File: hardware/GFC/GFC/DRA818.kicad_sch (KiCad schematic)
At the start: 28 parts

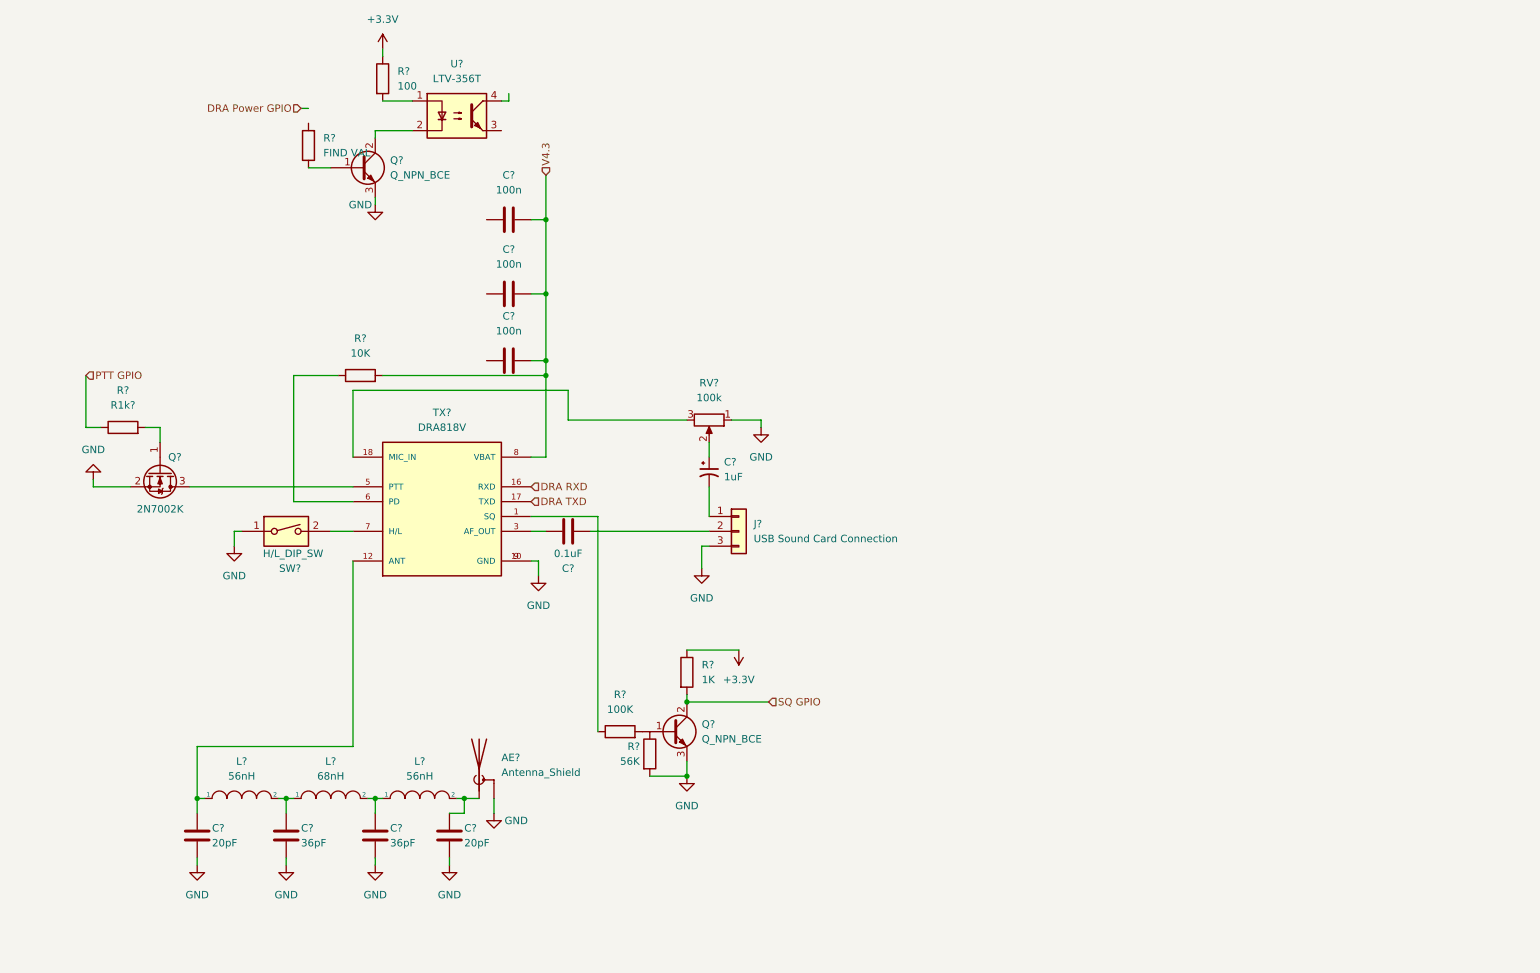
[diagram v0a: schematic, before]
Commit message: Some hardware changes, started to add footprints and part links to digikey. Switching most to SMD
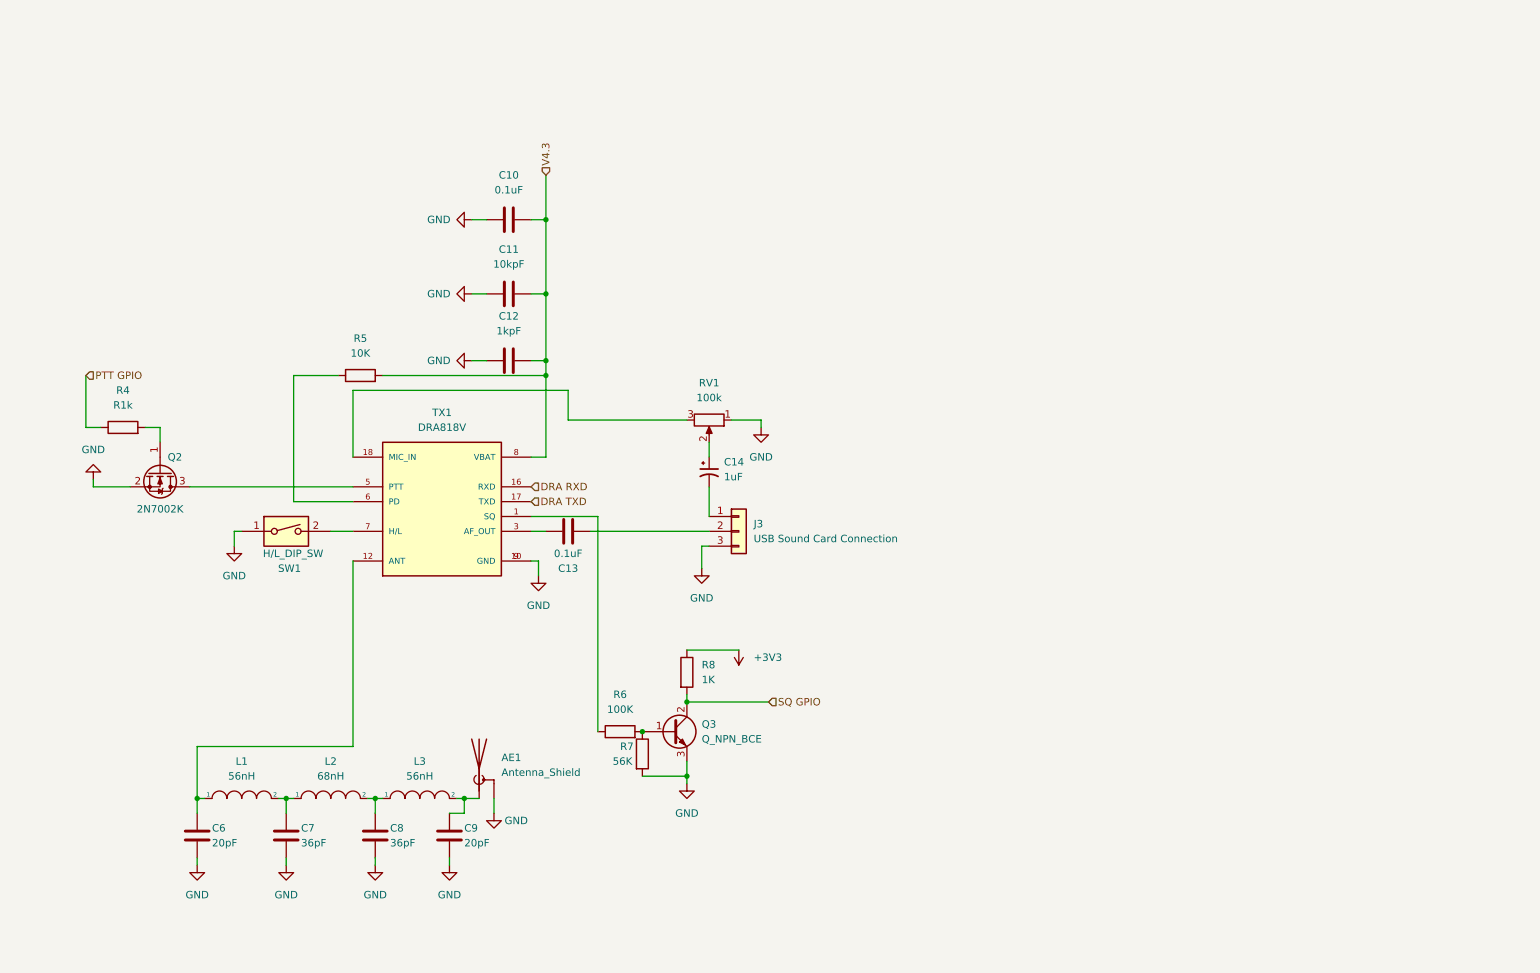
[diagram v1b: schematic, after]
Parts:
- removed Q?: Q_NPN_BCE, symbol Device:Q_NPN_BCE
- removed R?: 100, symbol Device:R
- removed R?: FIND VAL, symbol Device:R
- removed U?: LTV-356T, Package_SO:SO-4_4.4x3.6mm_P2.54mm, symbol Isolator:LTV-356T
- AE1: renamed from AE?; footprint (none) -> footprints:LINX_CONSMA001-G; Digikey (none) -> https://www.digikey.com/en/products/detail/linx-technologie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; Unit Price (none) -> 4.79
- C10: renamed from C?; value 100n -> 0.1uF; footprint (none) -> Capacitor_SMD:C_0603_1608Metric_Pad1.08x0.95mm_HandSolder; Digikey (none) -> https://www.digikey.com/short/3wn2fdb2; Unit Price (none) -> 0.10
- C11: renamed from C?; value 100n -> 10kpF; footprint (none) -> Capacitor_SMD:C_0603_1608Metric_Pad1.08x0.95mm_HandSolder; Digikey (none) -> https://www.digikey.com/short/0b20twhm; Unit Price (none) -> 0.10
- C12: renamed from C?; value 100n -> 1kpF; footprint (none) -> Capacitor_SMD:C_0603_1608Metric_Pad1.08x0.95mm_HandSolder; Digikey (none) -> https://www.digikey.com/short/wt1rq83j; Unit Price (none) -> 0.10
- C13: renamed from C?; footprint (none) -> Capacitor_SMD:C_0603_1608Metric_Pad1.08x0.95mm_HandSolder; Digikey (none) -> https://www.digikey.com/short/3wn2fdb2; Unit Price (none) -> 0.10
- C14: renamed from C?; footprint (none) -> Capacitor_SMD:C_0603_1608Metric_Pad1.08x0.95mm_HandSolder; Digikey (none) -> https://www.digikey.com/short/mb0p55bt; Unit Price (none) -> 0.10
- C6, C9: renamed from C?; footprint (none) -> Capacitor_SMD:C_0603_1608Metric_Pad1.08x0.95mm_HandSolder; Digikey (none) -> https://www.digikey.com/short/fmjn8mbp; Unit Price (none) -> 0.10
- C7, C8: renamed from C?; footprint (none) -> Capacitor_SMD:C_0603_1608Metric_Pad1.08x0.95mm_HandSolder; Digikey (none) -> https://www.digikey.com/short/327pncbq; Unit Price (none) -> 0.10
- J3: renamed from J?; footprint (none) -> Connector_PinHeader_2.54mm:PinHeader_1x03_P2.54mm_Vertical; Digikey (none) -> Already Have
- L1, L3: renamed from L?; footprint (none) -> footprints:IND_AIAC-1812-33NK-T; Digikey (none) -> https://www.digikey.com/short/9vrrnz3q; Unit Price (none) -> .67
- L2: renamed from L?; footprint (none) -> footprints:IND_AIAC-1812-33NK-T; Digikey (none) -> https://www.digikey.com/short/p9jjjhfr; Unit Price (none) -> .63
- Q2: renamed from Q?; footprint Package_TO_SOT_SMD:SOT-23 -> (none)
- R4: renamed from R?; value R1k? -> R1k; Field4 http://www.diygoodies.org.ua/wp-content/uploads/2017/11/Sch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 -> (none)
- RV1: renamed from RV?; footprint (none) -> footprints:TRIM_3361P-1-104GLF; Digikey (none) -> https://www.digikey.com/short/vp58mvrf
- SW1: renamed from SW?; footprint (none) -> Button_Switch_THT:SW_DIP_SPSTx01_Slide_6.7x4.1mm_W7.62mm_P2.54mm_LowProfile; Digikey (none) -> https://www.digikey.com/short/hh7p03qq; Unit Price (none) -> 0.42
- TX1: renamed from TX?; footprint DORJI_DRA818V -> footprints:DORJI_DRA818V; Digikey (none) -> eBay; Unit Price (none) -> 12.28
- gave numbers to parts that had none: 5
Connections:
- net GND: now also C10.1, C11.1, C12.1
- net at Q3.1 (B), R6.2: now also R7.1
- net +3.3V renamed +3V3
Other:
- moved on the sheet: R7

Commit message: Updated footprints - Started work on PCB layout
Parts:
- Q2: value 2N7002K -> DMN67D8LW-13; footprint (none) -> Package_TO_SOT_SMD:SOT-323_SC-70_Handsoldering; Digikey (none) -> https://www.digikey.com/short/vpj3wh87; Unit Price (none) -> 0.26
- Q3: footprint (none) -> Package_TO_SOT_SMD:SOT-23; Digikey (none) -> https://www.digikey.com/short/b477vdt4; Unit Price (none) -> $0.18
- R4: value R1k -> 10k; footprint (none) -> Resistor_SMD:R_0805_2012Metric_Pad1.20x1.40mm_HandSolder; Digikey (none) -> https://www.digikey.com/short/qp0zwmnj; Unit Price (none) -> 0.10
- R5: footprint (none) -> Resistor_SMD:R_0805_2012Metric_Pad1.20x1.40mm_HandSolder; Digikey (none) -> https://www.digikey.com/short/qp0zwmnj; Unit Price (none) -> 0.10
- R6: footprint (none) -> Resistor_SMD:R_0603_1608Metric_Pad0.98x0.95mm_HandSolder; Digikey (none) -> https://www.digikey.com/short/djq9jdpp; Unit Price (none) -> 0.10
- R7: footprint (none) -> Resistor_SMD:R_0603_1608Metric_Pad0.98x0.95mm_HandSolder; Digikey (none) -> https://www.digikey.com/short/bj31bf3h; Unit Price (none) -> 0.10
- R8: footprint (none) -> Resistor_SMD:R_0603_1608Metric_Pad0.98x0.95mm_HandSolder; Digikey (none) -> https://www.digikey.com/short/f10jtr77; Unit Price (none) -> 0.10
- RV1: Unit Price (none) -> 1.27
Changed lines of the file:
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@@
     (stroke (width 0) (type default) (color 0 0 0 0))
   )
-  (wire (pts (xy 33.02 99.06) (xy 39.37 99.06))
+  (wire (pts (xy 25.4 99.06) (xy 39.37 99.06))
     (stroke (width 0) (type default) (color 0 0 0 0))
   )
@@
   )
   (wire (pts (xy 66.04 152.4) (xy 67.31 152.4))
-    (stroke (width 0) (type default) (color 0 0 0 0))
-  )
-  (wire (pts (xy 33.02 99.06) (xy 33.02 97.79))
     (stroke (width 0) (type default) (color 0 0 0 0))
   )
@@
       (effects (font (size 1.27 1.27)) (justify left))
     )
-    (property "Footprint" "" (id 2) (at 132.842 130.81 90)
+    (property "Footprint" "Resistor_SMD:R_0603_1608Metric_Pad0.98x0.95mm_HandSolder" (id 2) (at 132.842 130.81 90)
       (effects (font (size 1.27 1.27)) hide)
     )
     (property "Datasheet" "~" (id 3) (at 134.62 130.81 0)
+      (effects (font (size 1.27 1.27)) hide)
+    )
+    (property "Digikey" "https://www.digikey.com/short/f10jtr77" (id 4) (at 134.62 130.81 0)
+      (effects (font (size 1.27 1.27)) hide)
+    )
+    (property "Unit Price" "0.10" (id 5) (at 134.62 130.81 0)
       (effects (font (size 1.27 1.27)) hide)
     )
@@
     (property "Reference" "R6" (id 0) (at 123.19 134.62 90))
     (property "Value" "100K" (id 1) (at 123.19 137.16 90))
-    (property "Footprint" "" (id 2) (at 123.19 142.748 90)
+    (property "Footprint" "Resistor_SMD:R_0603_1608Metric_Pad0.98x0.95mm_HandSolder" (id 2) (at 123.19 142.748 90)
       (effects (font (size 1.27 1.27)) hide)
     )
     (property "Datasheet" "~" (id 3) (at 123.19 140.97 0)
+      (effects (font (size 1.27 1.27)) hide)
+    )
+    (property "Digikey" "https://www.digikey.com/short/djq9jdpp" (id 4) (at 123.19 140.97 0)
+      (effects (font (size 1.27 1.27)) hide)
+    )
+    (property "Unit Price" "0.10" (id 5) (at 123.19 140.97 0)
       (effects (font (size 1.27 1.27)) hide)
     )
@@
       (effects (font (size 1.27 1.27)) hide)
     )
+    (property "Unit Price" "1.27" (id 5) (at 138.43 87.63 0)
+      (effects (font (size 1.27 1.27)) hide)
+    )
     (pin "1")
     (pin "2")
@@
     (property "Reference" "R5" (id 0) (at 78.74 73.66 90))
     (property "Value" "10K" (id 1) (at 78.74 76.2 90))
-    (property "Footprint" "" (id 2) (at 78.74 81.788 90)
+    (property "Footprint" "Resistor_SMD:R_0805_2012Metric_Pad1.20x1.40mm_HandSolder" (id 2) (at 78.74 81.788 90)
       (effects (font (size 1.27 1.27)) hide)
     )
@@
       (effects (font (size 1.27 1.27)) hide)
     )
+    (property "Digikey" "https://www.digikey.com/short/qp0zwmnj" (id 4) (at 78.74 80.01 0)
+      (effects (font (size 1.27 1.27)) hide)
+    )
+    (property "Unit Price" "0.10" (id 5) (at 78.74 80.01 0)
+      (effects (font (size 1.27 1.27)) hide)
+    )
     (pin "1")
     (pin "2")
@@
     (in_bom yes) (on_board yes)
     (property "Reference" "Q2" (id 0) (at 46.99 93.98 90))
-    (property "Value" "2N7002K" (id 1) (at 44.45 102.87 90))
-    (property "Footprint" "" (id 2) (at 42.545 101.6 0)
+    (property "Value" "DMN67D8LW-13" (id 1) (at 44.45 102.87 90))
+    (property "Footprint" "Package_TO_SOT_SMD:SOT-323_SC-70_Handsoldering" (id 2) (at 42.545 101.6 0)
       (effects (font (size 1.27 1.27) italic) (justify left) hide)
     )
     (property "Datasheet" "https://www.diodes.com/assets/Datasheets/ds30896.pdf" (id 3) (at 44.45 96.52 0)
       (effects (font (size 1.27 1.27)) (justify left) hide)
+    )
+    (property "Digikey" "https://www.digikey.com/short/vpj3wh87" (id 4) (at 44.45 96.52 0)
+      (effects (font (size 1.27 1.27)) hide)
+    )
+    (property "Unit Price" "0.26" (id 5) (at 44.45 96.52 0)
+      (effects (font (size 1.27 1.27)) hide)
     )
     (pin "1")
@@
       (effects (font (size 1.27 1.27)) (justify left))
     )
-    (property "Footprint" "" (id 2) (at 137.16 138.43 0)
+    (property "Footprint" "Package_TO_SOT_SMD:SOT-23" (id 2) (at 137.16 138.43 0)
       (effects (font (size 1.27 1.27)) hide)
     )
@@
       (effects (font (size 1.27 1.27)) hide)
     )
+    (property "Digikey" "https://www.digikey.com/short/b477vdt4" (id 4) (at 132.08 140.97 0)
+      (effects (font (size 1.27 1.27)) hide)
+    )
+    (property "Unit Price" "$0.18" (id 5) (at 132.08 140.97 0)
+      (effects (font (size 1.27 1.27)) hide)
+    )
     (pin "1")
     (pin "2")
@@
       (effects (font (size 1.27 1.27)) (justify left))
     )
-    (property "Footprint" "" (id 2) (at 125.222 144.78 90)
+    (property "Footprint" "Resistor_SMD:R_0603_1608Metric_Pad0.98x0.95mm_HandSolder" (id 2) (at 125.222 144.78 90)
       (effects (font (size 1.27 1.27)) hide)
     )
@@
       (effects (font (size 1.27 1.27)) hide)
     )
-    (pin "1")
-    (pin "2")
-  )
-  (symbol (lib_id "power:GND") (at 33.02 97.79 180) (unit 1)
-    (in_bom yes) (on_board yes) (fields_autoplaced)
-    (property "Reference" "#PWR0132" (id 0) (at 33.02 91.44 0)
-      (effects (font (size 1.27 1.27)) hide)
-    )
-    (property "Value" "GND" (id 1) (at 33.02 92.71 0))
-    (property "Footprint" "" (id 2) (at 33.02 97.79 0)
-      (effects (font (size 1.27 1.27)) hide)
-    )
-    (property "Datasheet" "" (id 3) (at 33.02 97.79 0)
+    (property "Digikey" "https://www.digikey.com/short/bj31bf3h" (id 4) (at 127 144.78 0)
+      (effects (font (size 1.27 1.27)) hide)
+    )
+    (property "Unit Price" "0.10" (id 5) (at 127 144.78 0)
+      (effects (font (size 1.27 1.27)) hide)
+    )
+    (pin "1")
+    (pin "2")
+  )
+  (symbol (lib_id "power:GND") (at 25.4 99.06 0) (unit 1)
+    (in_bom yes) (on_board yes) (fields_autoplaced)
+    (property "Reference" "#PWR0132" (id 0) (at 25.4 105.41 0)
+      (effects (font (size 1.27 1.27)) hide)
+    )
+    (property "Value" "GND" (id 1) (at 25.4 104.14 0))
+    (property "Footprint" "" (id 2) (at 25.4 99.06 0)
+      (effects (font (size 1.27 1.27)) hide)
+    )
+    (property "Datasheet" "" (id 3) (at 25.4 99.06 0)
       (effects (font (size 1.27 1.27)) hide)
     )
@@
     (in_bom yes) (on_board yes) (fields_autoplaced)
     (property "Reference" "R4" (id 0) (at 38.1 82.55 90))
-    (property "Value" "R1k" (id 1) (at 38.1 85.09 90))
-    (property "Footprint" "" (id 2) (at 38.1 90.678 90)
+    (property "Value" "10k" (id 1) (at 38.1 85.09 90))
+    (property "Footprint" "Resistor_SMD:R_0805_2012Metric_Pad1.20x1.40mm_HandSolder" (id 2) (at 38.1 90.678 90)
       (effects (font (size 1.27 1.27)) hide)
     )
@@
       (effects (font (size 1.27 1.27)) hide)
     )
+    (property "Digikey" "https://www.digikey.com/short/qp0zwmnj" (id 5) (at 38.1 88.9 0)
+      (effects (font (size 1.27 1.27)) hide)
+    )
+    (property "Unit Price" "0.10" (id 6) (at 38.1 88.9 0)
+      (effects (font (size 1.27 1.27)) hide)
+    )

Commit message: Sync PCB
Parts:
- removed AE1: Antenna_Shield, footprints:LINX_CONSMA001-G, symbol Device:Antenna_Shield
- added AE1: Antenna, footprints:LINX_CONSMA001-G, symbol Device:Antenna
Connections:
- net at C9.1, L3.2: now also AE1.1 (A)
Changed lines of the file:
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@@
-    (stroke (width 0) (type default) (color 0 0 0 0))
-  )
-  (wire (pts (xy 101.6 152.4) (xy 101.6 154.94))
     (stroke (width 0) (type default) (color 0 0 0 0))
   )
@@
   )
   (wire (pts (xy 134.62 148.59) (xy 134.62 149.86))
+    (stroke (width 0) (type default) (color 0 0 0 0))
+  )
+  (wire (pts (xy 99.06 148.59) (xy 99.06 152.4))
     (stroke (width 0) (type default) (color 0 0 0 0))
   )
@@
     (pin "3")
   )
-  (symbol (lib_id "power:GND") (at 101.6 154.94 0) (unit 1)
-    (in_bom yes) (on_board yes)
-    (property "Reference" "#PWR0124" (id 0) (at 101.6 161.29 0)
-      (effects (font (size 1.27 1.27)) hide)
-    )
-    (property "Value" "GND" (id 1) (at 105.41 156.21 0))
-    (property "Footprint" "" (id 2) (at 101.6 154.94 0)
-      (effects (font (size 1.27 1.27)) hide)
-    )
-    (property "Datasheet" "" (id 3) (at 101.6 154.94 0)
-      (effects (font (size 1.27 1.27)) hide)
-    )
-    (pin "1")
-  )
   (symbol (lib_id "power:GND") (at 50.8 163.83 0) (unit 1)
     (in_bom yes) (on_board yes) (fields_autoplaced)
@@
     (pin "2")
   )
+  (symbol (lib_id "Device:Antenna") (at 99.06 143.51 0) (unit 1)
+    (in_bom yes) (on_board yes) (fields_autoplaced)
+    (property "Reference" "AE1" (id 0) (at 101.6 142.8749 0)
+      (effects (font (size 1.27 1.27)) (justify left))
+    )
+    (property "Value" "Antenna" (id 1) (at 101.6 145.4149 0)
+      (effects (font (size 1.27 1.27)) (justify left))
+    )
+    (property "Footprint" "footprints:LINX_CONSMA001-G" (id 2) (at 99.06 143.51 0)
+      (effects (font (size 1.27 1.27)) hide)
+    )
+    (property "Datasheet" "~" (id 3) (at 99.06 143.51 0)
+      (effects (font (size 1.27 1.27)) hide)
+    )
+    (pin "1")
+  )
   (symbol (lib_id "Device:C") (at 93.98 158.75 0) (unit 1)
     (in_bom yes) (on_board yes)
@@
     (pin "1")
   )
-  (symbol (lib_id "Device:Antenna_Shield") (at 99.06 147.32 0) (unit 1)
-    (in_bom yes) (on_board yes) (fields_autoplaced)
-    (property "Reference" "AE1" (id 0) (at 102.87 145.4149 0)
-      (effects (font (size 1.27 1.27)) (justify left))
-    )
-    (property "Value" "Antenna_Shield" (id 1) (at 102.87 147.9549 0)
-      (effects (font (size 1.27 1.27)) (justify left))
-    )
-    (property "Footprint" "footprints:LINX_CONSMA001-G" (id 2) (at 99.06 144.78 0)
-      (effects (font (size 1.27 1.27)) hide)
-    )
-    (property "Datasheet" "https://www.digikey.com/en/products/detail/linx-technologies-inc/CONSMA001-G/5012143?utm_source=snapeda&utm_medium=aggregator&utm_campaign=buynow" (id 3) (at 99.06 144.78 0)
-      (effects (font (size 1.27 1.27)) hide)
-    )
-    (property "Digikey" "https://www.digikey.com/en/products/detail/linx-technologies-inc/CONSMA001-G/5012143" (id 4) (at 99.06 147.32 0)
-      (effects (font (size 1.27 1.27)) hide)
-    )
-    (property "Unit Price" "4.79" (id 5) (at 99.06 147.32 0)
-      (effects (font (size 1.27 1.27)) hide)
-    )
-    (pin "1")
-    (pin "2")
-  )
   (symbol (lib_id "Switch:SW_DIP_x01") (at 66.04 106.68 0) (unit 1)
